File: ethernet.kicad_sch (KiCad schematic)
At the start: 64 parts, among them Q6001 DMG1012T, Q6002 DMG1012T, U1001 AM6231ASGGGAALW, U6001 HR911130A, U6002 RTL8211F-CG

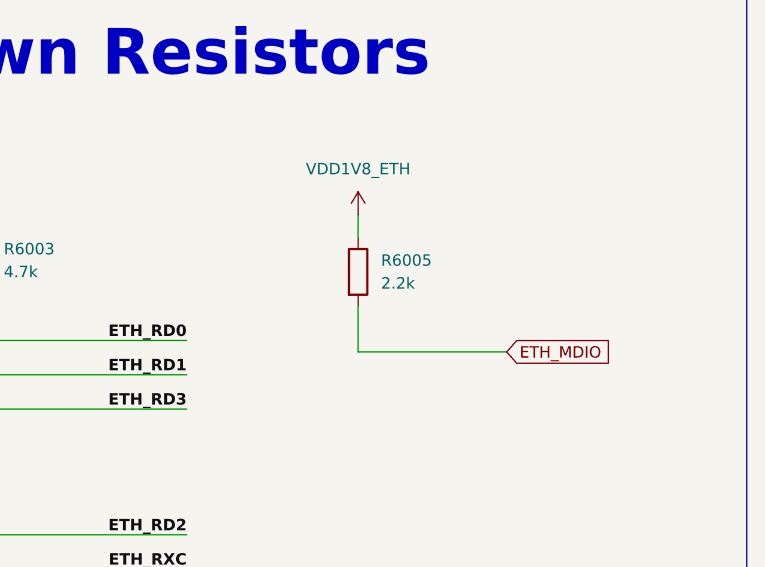
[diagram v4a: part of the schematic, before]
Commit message: Routed most of Ethernet PHY and RGMII
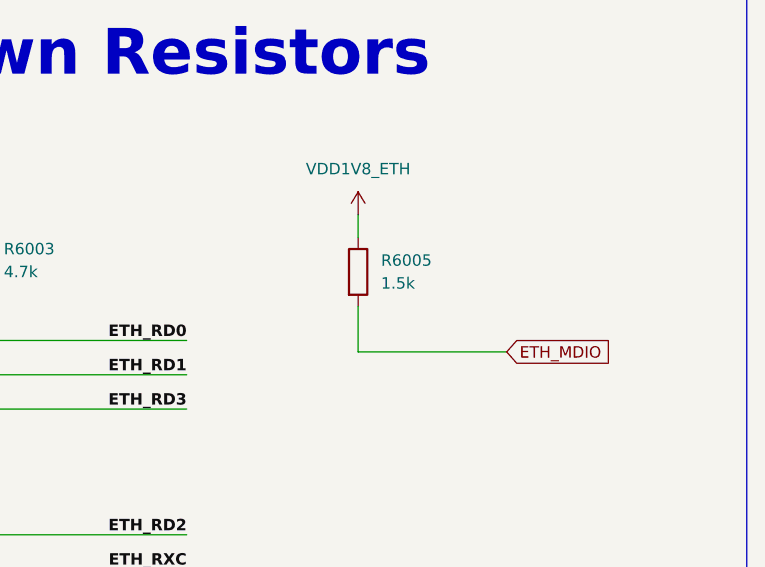
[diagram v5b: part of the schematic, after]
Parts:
- C6001, C6002, C6004, C6005, C6017, C6019, C6020: footprint Capacitor_SMD:C_0201_0603Metric -> Capacitor_SMD:C_0402_1005Metric
- R6001, R6002, R6003, R6006, R6007, R6008, R6009, R6010, R6011, R6012, R6013, R6014, R6015, R6016, R6017, R6018, R6019, R6020, R6021: footprint Resistor_SMD:R_0201_0603Metric -> Resistor_SMD:R_0402_1005Metric
- R6004: footprint Resistor_SMD:R_1206_3216Metric -> Resistor_SMD:R_0402_1005Metric
- R6005: value 2.2k -> 1.5k; footprint Resistor_SMD:R_0201_0603Metric -> Resistor_SMD:R_0402_1005Metric
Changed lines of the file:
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@@
 			)
 		)
-		(property "Footprint" "Resistor_SMD:R_0201_0603Metric"
+		(property "Footprint" "Resistor_SMD:R_0402_1005Metric"
 			(at 240.03 184.658 90)
 			(effects
@@
 			)
 		)
-		(property "Value" "2.2k"
+		(property "Value" "1.5k"
 			(at 581.66 109.2199 0)
 			(effects
@@
 			)
 		)
-		(property "Footprint" "Resistor_SMD:R_0201_0603Metric"
+		(property "Footprint" "Resistor_SMD:R_0402_1005Metric"
 			(at 577.342 107.95 90)
 			(effects
@@
 			)
 		)
-		(property "Footprint" "Resistor_SMD:R_0201_0603Metric"
+		(property "Footprint" "Resistor_SMD:R_0402_1005Metric"
 			(at 240.03 187.198 90)
 			(effects
@@
 			)
 		)
-		(property "Footprint" "Resistor_SMD:R_1206_3216Metric"
+		(property "Footprint" "Resistor_SMD:R_0402_1005Metric"
 			(at 427.99 291.338 90)
 			(effects
@@
 			)
 		)
-		(property "Footprint" "Resistor_SMD:R_0201_0603Metric"
+		(property "Footprint" "Resistor_SMD:R_0402_1005Metric"
 			(at 144.78 211.328 90)
 			(effects
@@
 			)
 		)
-		(property "Footprint" "Resistor_SMD:R_0201_0603Metric"
+		(property "Footprint" "Resistor_SMD:R_0402_1005Metric"
 			(at 144.78 208.788 90)
 			(effects
@@
 			)
 		)
-		(property "Footprint" "Capacitor_SMD:C_0201_0603Metric"
+		(property "Footprint" "Capacitor_SMD:C_0402_1005Metric"
 			(at 376.2248 106.68 0)
 			(effects
@@
 			)
 		)
-		(property "Footprint" "Resistor_SMD:R_0201_0603Metric"
+		(property "Footprint" "Resistor_SMD:R_0402_1005Metric"
 			(at 240.03 196.088 90)
 			(effects
@@
 			)
 		)
-		(property "Footprint" "Capacitor_SMD:C_0201_0603Metric"
+		(property "Footprint" "Capacitor_SMD:C_0402_1005Metric"
 			(at 396.5448 106.68 0)
 			(effects
@@
 			)
 		)
-		(property "Footprint" "Resistor_SMD:R_0201_0603Metric"
+		(property "Footprint" "Resistor_SMD:R_0402_1005Metric"
 			(at 240.03 189.738 90)
 			(effects
@@
 			)
 		)
-		(property "Footprint" "Resistor_SMD:R_0201_0603Metric"
+		(property "Footprint" "Resistor_SMD:R_0402_1005Metric"
 			(at 525.272 153.67 90)
 			(effects
@@
 			)
 		)
-		(property "Footprint" "Resistor_SMD:R_0201_0603Metric"
+		(property "Footprint" "Resistor_SMD:R_0402_1005Metric"
 			(at 515.112 153.67 90)
 			(effects
@@
 			)
 		)
-		(property "Footprint" "Resistor_SMD:R_0201_0603Metric"
+		(property "Footprint" "Resistor_SMD:R_0402_1005Metric"
 			(at 144.78 218.948 90)
 			(effects
@@
 			)
 		)
-		(property "Footprint" "Capacitor_SMD:C_0201_0603Metric"
+		(property "Footprint" "Capacitor_SMD:C_0402_1005Metric"
 			(at 334.9752 106.68 0)
 			(effects
@@
 			)
 		)
-		(property "Footprint" "Capacitor_SMD:C_0201_0603Metric"
+		(property "Footprint" "Capacitor_SMD:C_0402_1005Metric"
 			(at 270.2052 168.91 0)
 			(effects
@@
 			)
 		)
-		(property "Footprint" "Capacitor_SMD:C_0201_0603Metric"
+		(property "Footprint" "Capacitor_SMD:C_0402_1005Metric"
 			(at 228.2952 242.57 0)
 			(effects
@@
 			)
 		)
-		(property "Footprint" "Capacitor_SMD:C_0201_0603Metric"
+		(property "Footprint" "Capacitor_SMD:C_0402_1005Metric"
 			(at 322.2752 106.68 0)
 			(effects
@@
 			)
 		)
-		(property "Footprint" "Resistor_SMD:R_0201_0603Metric"
+		(property "Footprint" "Resistor_SMD:R_0402_1005Metric"
 			(at 525.272 106.68 90)
 			(effects
@@
 			)
 		)
-		(property "Footprint" "Resistor_SMD:R_0201_0603Metric"
+		(property "Footprint" "Resistor_SMD:R_0402_1005Metric"
 			(at 240.03 192.278 90)
 			(effects
@@
 			)
 		)
-		(property "Footprint" "Resistor_SMD:R_0201_0603Metric"
+		(property "Footprint" "Resistor_SMD:R_0402_1005Metric"
 			(at 515.112 106.68 90)
 			(effects
@@
 			)
 		)
-		(property "Footprint" "Resistor_SMD:R_0201_0603Metric"
+		(property "Footprint" "Resistor_SMD:R_0402_1005Metric"
 			(at 144.78 203.708 90)
 			(effects
@@
 			)
 		)
-		(property "Footprint" "Capacitor_SMD:C_0201_0603Metric"
+		(property "Footprint" "Capacitor_SMD:C_0402_1005Metric"
 			(at 381.9652 170.18 0)
 			(effects
@@
 			)
 		)
-		(property "Footprint" "Resistor_SMD:R_0201_0603Metric"
+		(property "Footprint" "Resistor_SMD:R_0402_1005Metric"
 			(at 144.78 215.138 90)
 			(effects
@@
 			)
 		)
-		(property "Footprint" "Resistor_SMD:R_0201_0603Metric"
+		(property "Footprint" "Resistor_SMD:R_0402_1005Metric"
 			(at 249.428 248.92 90)
 			(effects
@@
 			)
 		)
-		(property "Footprint" "Resistor_SMD:R_0201_0603Metric"
+		(property "Footprint" "Resistor_SMD:R_0402_1005Metric"
 			(at 144.78 206.248 90)
 			(effects
@@
 			)
 		)
-		(property "Footprint" "Resistor_SMD:R_0201_0603Metric"
+		(property "Footprint" "Resistor_SMD:R_0402_1005Metric"
 			(at 240.03 199.898 90)
 			(effects
@@
 			)
 		)
-		(property "Footprint" "Resistor_SMD:R_0201_0603Metric"
+		(property "Footprint" "Resistor_SMD:R_0402_1005Metric"
 			(at 535.432 153.67 90)
 			(effects
@@
 			)
 		)
-		(property "Footprint" "Resistor_SMD:R_0201_0603Metric"
+		(property "Footprint" "Resistor_SMD:R_0402_1005Metric"
 			(at 535.432 106.68 90)
 			(effects

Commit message: Continued routing Ethernet PHY external circuitry. Added ESD protection diode arrays to Ethernet
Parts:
- removed TP6001: TestPoint, TestPoint:TestPoint_Pad_1.0x1.0mm, symbol Connector:TestPoint
- added U6003, U6004: TPD4E05U06DQA, Package_SON:USON-10_2.5x1.0mm_P0.5mm, symbol Power_Protection:TPD4E05U06DQA
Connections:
- net ETH_MD0+: now also U6004.4 (D2+)
- net ETH_MD0-: now also U6004.5 (D2-)
- net ETH_MD1+: now also U6004.1 (D1+)
- net ETH_MD1-: now also U6004.2 (D1-)
- net ETH_MD2+: now also U6003.4 (D2+)
- net ETH_MD2-: now also U6003.5 (D2-)
- net ETH_MD3+: now also U6003.1 (D1+)
- net ETH_MD3-: now also U6003.2 (D1-)
- net GND: now also U6003.3 (GND), U6003.8 (GND)
- net ETH_CLKOUT: no longer names the net of U6002.35 (CLK_OUT)
- new net: U6004.3 (GND), U6004.8 (GND)
- no-connect marks 13 -> 14
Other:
- moved on the sheet: C6022, R6001, R6002, R6003, R6004, R6005, R6006, R6007, R6008, R6026, R6027, U6001

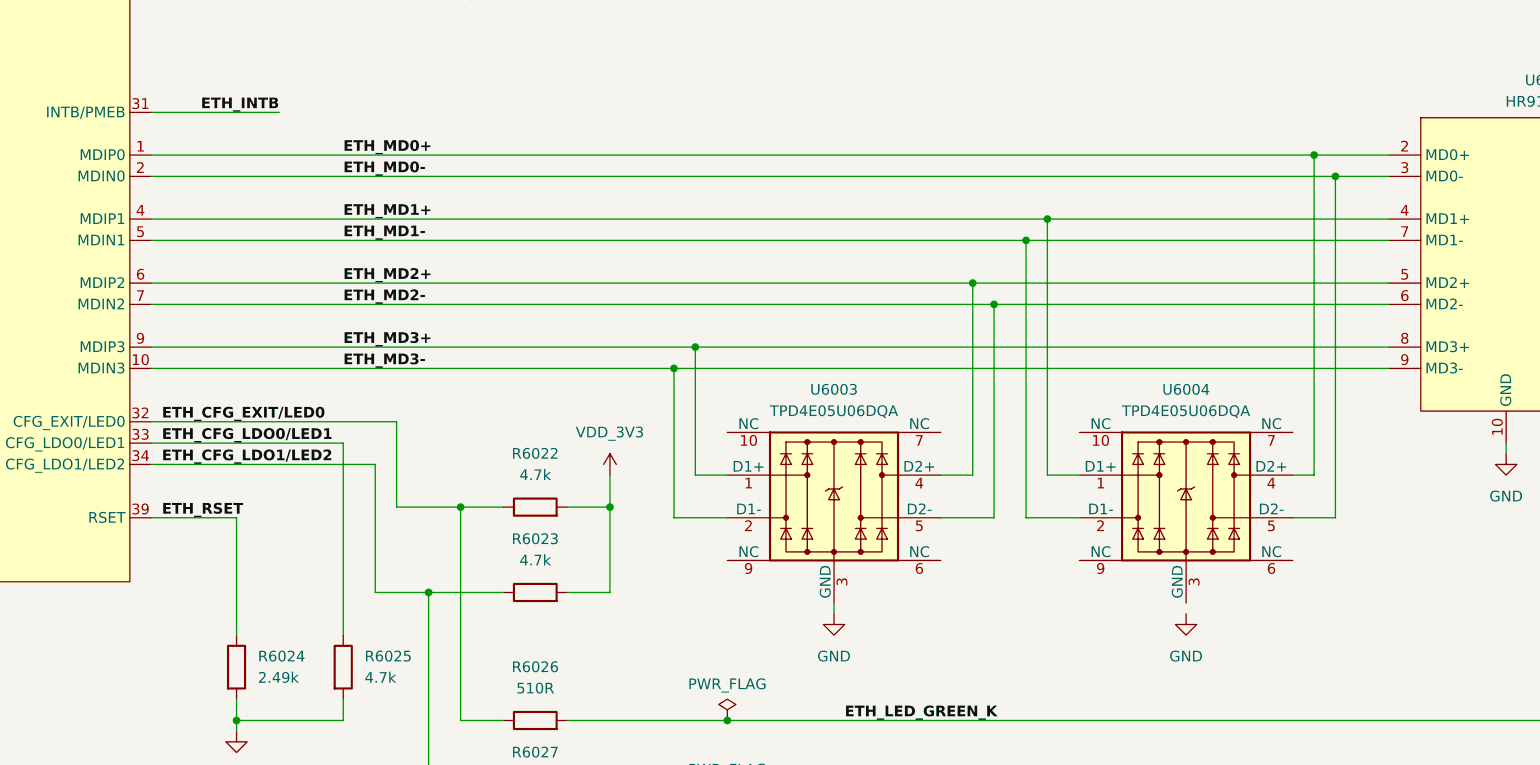
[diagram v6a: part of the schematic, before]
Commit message: Length tuned Ethernet lines
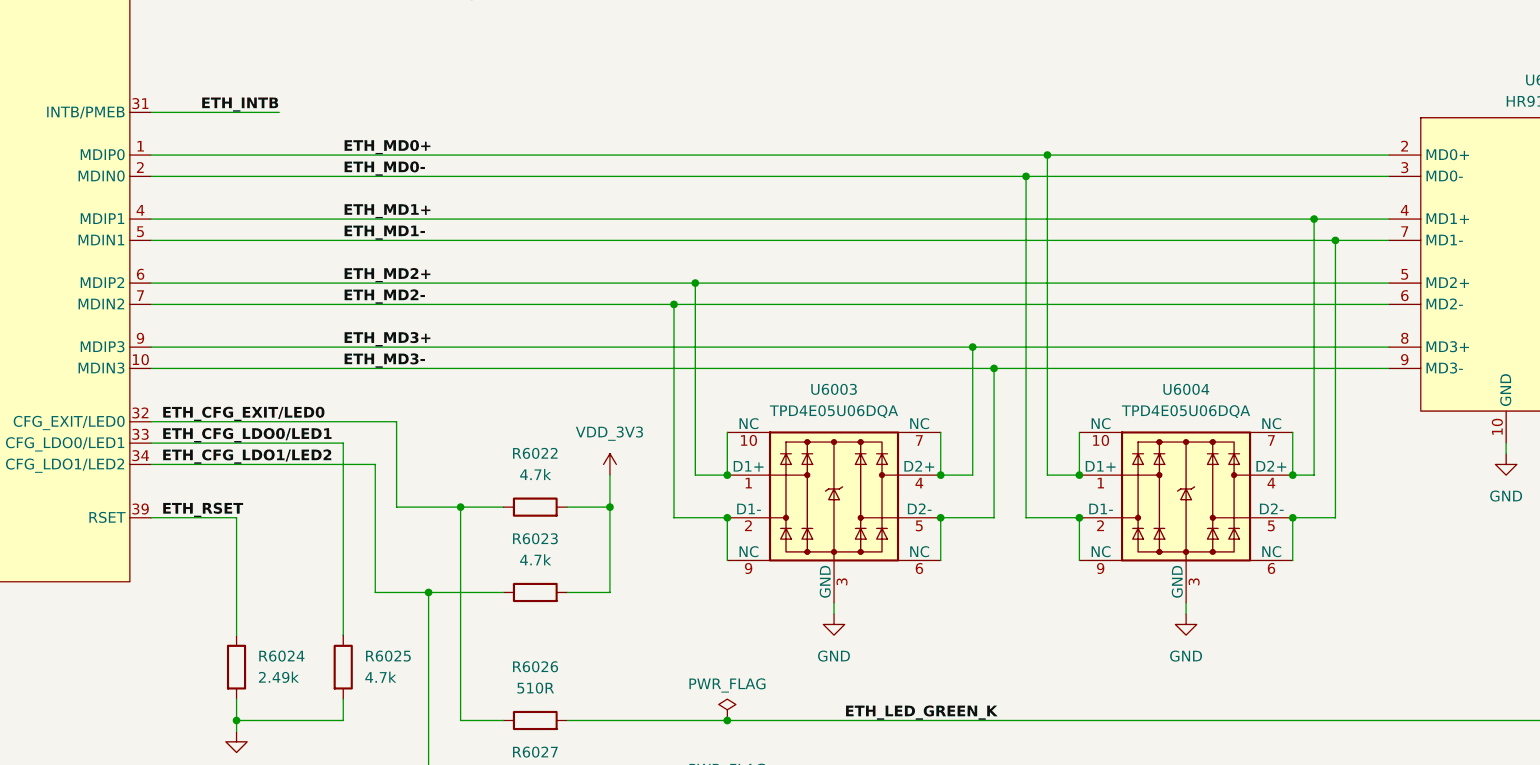
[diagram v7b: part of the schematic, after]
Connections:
- net ETH_MD0+: now also U6004.1 (D1+), U6004.10 (NC); no longer U6004.4 (D2+)
- net ETH_MD0-: now also U6004.2 (D1-), U6004.9 (NC); no longer U6004.5 (D2-)
- net ETH_MD1+: now also U6004.4 (D2+), U6004.7 (NC); no longer U6004.1 (D1+)
- net ETH_MD1-: now also U6004.5 (D2-), U6004.6 (NC); no longer U6004.2 (D1-)
- net ETH_MD2+: now also U6003.1 (D1+), U6003.10 (NC); no longer U6003.4 (D2+)
- net ETH_MD2-: now also U6003.2 (D1-), U6003.9 (NC); no longer U6003.5 (D2-)
- net ETH_MD3+: now also U6003.4 (D2+), U6003.7 (NC); no longer U6003.1 (D1+)
- net ETH_MD3-: now also U6003.5 (D2-), U6003.6 (NC); no longer U6003.2 (D1-)
- net GND: now also U6004.3 (GND), U6004.8 (GND)

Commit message: Routed eMMC and finished length tuning RGMII
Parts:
- C6007, C6008, C6009, C6010, C6015: footprint Capacitor_SMD:C_0201_0603Metric -> Capacitor_SMD:C_0402_1005Metric
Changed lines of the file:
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@@
 			)
 		)
-		(property "Footprint" "Capacitor_SMD:C_0201_0603Metric"
+		(property "Footprint" "Capacitor_SMD:C_0402_1005Metric"
 			(at 371.8052 139.7 0)
 			(effects
@@
 			)
 		)
-		(property "Footprint" "Capacitor_SMD:C_0201_0603Metric"
+		(property "Footprint" "Capacitor_SMD:C_0402_1005Metric"
 			(at 266.3952 140.97 0)
 			(effects
@@
 			)
 		)
-		(property "Footprint" "Capacitor_SMD:C_0201_0603Metric"
+		(property "Footprint" "Capacitor_SMD:C_0402_1005Metric"
 			(at 360.3752 139.7 0)
 			(effects
@@
 			)
 		)
-		(property "Footprint" "Capacitor_SMD:C_0201_0603Metric"
+		(property "Footprint" "Capacitor_SMD:C_0402_1005Metric"
 			(at 169.8752 130.81 0)
 			(effects
@@
 			)
 		)
-		(property "Footprint" "Capacitor_SMD:C_0201_0603Metric"
+		(property "Footprint" "Capacitor_SMD:C_0402_1005Metric"
 			(at 347.6752 139.7 0)
 			(effects
